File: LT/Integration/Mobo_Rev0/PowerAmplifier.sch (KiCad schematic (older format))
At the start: 12 parts, among them Q3 Q_NPN_BEC, Q4 Q_PNP_BEC, T1 TC2-1T+, T2 TC2-1T+

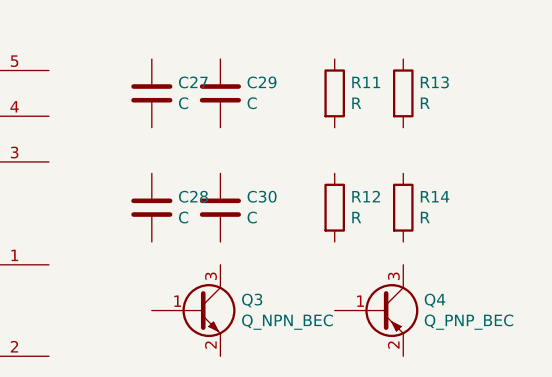
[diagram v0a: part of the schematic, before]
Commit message: I uploaded the schematics for the receiving stage into their respective hierarchial sheets and have begun the integration of the received stage
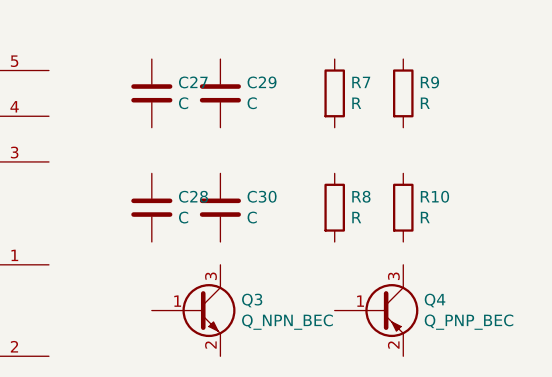
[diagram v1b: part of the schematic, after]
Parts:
- C27, C28, C29, C30: footprint Capacitor_SMD:C_0805_2012Metric -> (none)
- Q3, Q4: footprint Package_TO_SOT_SMD:SOT-23_Handsoldering -> (none)
- R10: renamed from R14; footprint Capacitor_SMD:C_0805_2012Metric -> (none)
- R7: renamed from R11; footprint Capacitor_SMD:C_0805_2012Metric -> (none)
- R8: renamed from R12; footprint Capacitor_SMD:C_0805_2012Metric -> (none)
- R9: renamed from R13; footprint Capacitor_SMD:C_0805_2012Metric -> (none)
- T1, T2: footprint Transformer_SMD:Transformer_MACOM_SM-22 -> (none)
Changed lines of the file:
@@
 F 0 "C27" H 4865 1446 50  0000 L CNN
 F 1 "C" H 4865 1355 50  0000 L CNN
-F 2 "Capacitor_SMD:C_0805_2012Metric" H 4788 1250 50  0001 C CNN
+F 2 "" H 4788 1250 50  0001 C CNN
 F 3 "~" H 4750 1400 50  0001 C CNN
 	1    4750 1400
@@
 F 0 "C29" H 5165 1446 50  0000 L CNN
 F 1 "C" H 5165 1355 50  0000 L CNN
-F 2 "Capacitor_SMD:C_0805_2012Metric" H 5088 1250 50  0001 C CNN
+F 2 "" H 5088 1250 50  0001 C CNN
 F 3 "~" H 5050 1400 50  0001 C CNN
 	1    5050 1400
@@
 F 0 "C28" H 4865 1946 50  0000 L CNN
 F 1 "C" H 4865 1855 50  0000 L CNN
-F 2 "Capacitor_SMD:C_0805_2012Metric" H 4788 1750 50  0001 C CNN
+F 2 "" H 4788 1750 50  0001 C CNN
 F 3 "~" H 4750 1900 50  0001 C CNN
 	1    4750 1900
@@
 F 0 "C30" H 5165 1946 50  0000 L CNN
 F 1 "C" H 5165 1855 50  0000 L CNN
-F 2 "Capacitor_SMD:C_0805_2012Metric" H 5088 1750 50  0001 C CNN
+F 2 "" H 5088 1750 50  0001 C CNN
 F 3 "~" H 5050 1900 50  0001 C CNN
 	1    5050 1900
@@
 $EndComp
 $Comp
-L Device:R R11
+L Device:R R7
 U 1 1 5E4C4AC0
 P 5550 1400
-F 0 "R11" H 5620 1446 50  0000 L CNN
+F 0 "R7" H 5620 1446 50  0000 L CNN
 F 1 "R" H 5620 1355 50  0000 L CNN
-F 2 "Capacitor_SMD:C_0805_2012Metric" V 5480 1400 50  0001 C CNN
+F 2 "" V 5480 1400 50  0001 C CNN
 F 3 "~" H 5550 1400 50  0001 C CNN
 	1    5550 1400
@@
 $EndComp
 $Comp
-L Device:R R13
+L Device:R R9
 U 1 1 5E4C4B1C
 P 5850 1400
-F 0 "R13" H 5920 1446 50  0000 L CNN
+F 0 "R9" H 5920 1446 50  0000 L CNN
 F 1 "R" H 5920 1355 50  0000 L CNN
-F 2 "Capacitor_SMD:C_0805_2012Metric" V 5780 1400 50  0001 C CNN
+F 2 "" V 5780 1400 50  0001 C CNN
 F 3 "~" H 5850 1400 50  0001 C CNN
 	1    5850 1400
@@
 $EndComp
 $Comp
-L Device:R R12
+L Device:R R8
 U 1 1 5E4C4B5D
 P 5550 1900
-F 0 "R12" H 5620 1946 50  0000 L CNN
+F 0 "R8" H 5620 1946 50  0000 L CNN
 F 1 "R" H 5620 1855 50  0000 L CNN
-F 2 "Capacitor_SMD:C_0805_2012Metric" V 5480 1900 50  0001 C CNN
+F 2 "" V 5480 1900 50  0001 C CNN
 F 3 "~" H 5550 1900 50  0001 C CNN
 	1    5550 1900
@@
 $EndComp
 $Comp
-L Device:R R14
+L Device:R R10
 U 1 1 5E4C4BA1
 P 5850 1900
-F 0 "R14" H 5920 1946 50  0000 L CNN
+F 0 "R10" H 5920 1946 50  0000 L CNN
 F 1 "R" H 5920 1855 50  0000 L CNN
-F 2 "Capacitor_SMD:C_0805_2012Metric" V 5780 1900 50  0001 C CNN
+F 2 "" V 5780 1900 50  0001 C CNN
 F 3 "~" H 5850 1900 50  0001 C CNN
 	1    5850 1900
@@
 F 0 "T1" H 3900 1878 50  0000 C CNN
 F 1 "TC2-1T+" H 3900 1787 50  0000 C CNN
-F 2 "Transformer_SMD:Transformer_MACOM_SM-22" H 3900 1500 50  0001 C CNN
+F 2 "" H 3900 1500 50  0001 C CNN
 F 3 "~" H 3900 1500 50  0001 C CNN
 	1    3900 1500
@@
 F 0 "T2" H 3900 2728 50  0000 C CNN
 F 1 "TC2-1T+" H 3900 2637 50  0000 C CNN
-F 2 "Transformer_SMD:Transformer_MACOM_SM-22" H 3900 2350 50  0001 C CNN
+F 2 "" H 3900 2350 50  0001 C CNN
 F 3 "~" H 3900 2350 50  0001 C CNN
 	1    3900 2350
@@
 F 0 "Q3" H 5141 2396 50  0000 L CNN
 F 1 "Q_NPN_BEC" H 5141 2305 50  0000 L CNN
-F 2 "Package_TO_SOT_SMD:SOT-23_Handsoldering" H 5150 2450 50  0001 C CNN
+F 2 "" H 5150 2450 50  0001 C CNN
 F 3 "~" H 4950 2350 50  0001 C CNN
 	1    4950 2350
@@
 F 0 "Q4" H 5940 2396 50  0000 L CNN
 F 1 "Q_PNP_BEC" H 5940 2305 50  0000 L CNN
-F 2 "Package_TO_SOT_SMD:SOT-23_Handsoldering" H 5950 2450 50  0001 C CNN
+F 2 "" H 5950 2450 50  0001 C CNN
 F 3 "~" H 5750 2350 50  0001 C CNN
 	1    5750 2350

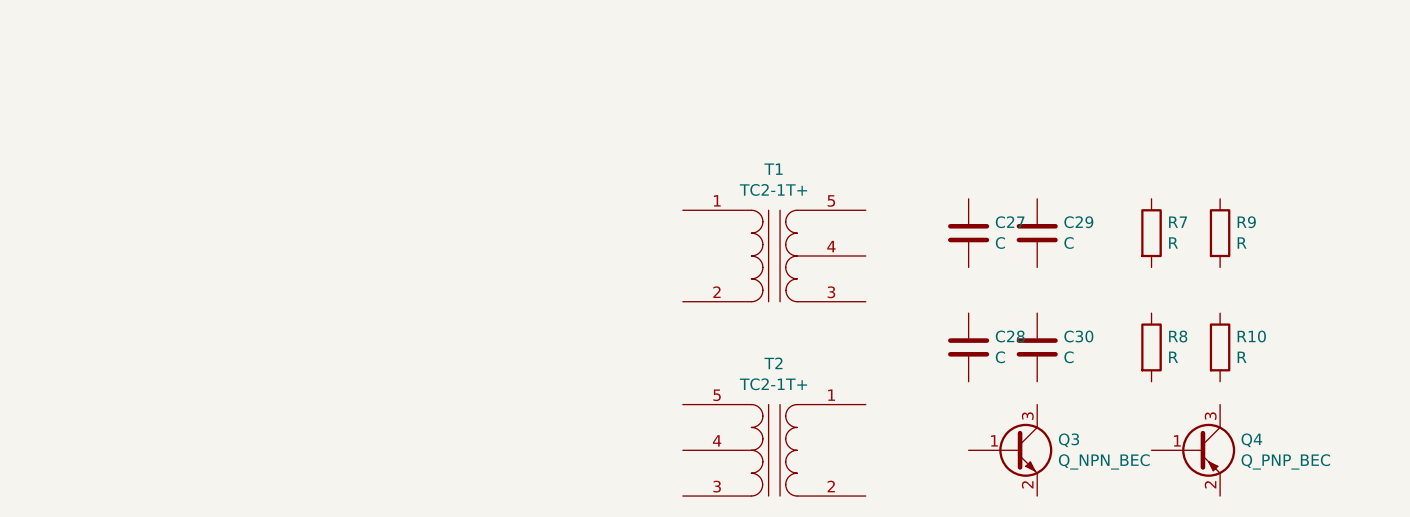
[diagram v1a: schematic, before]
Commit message: Uploaded Schematics to Integration of Phase 2
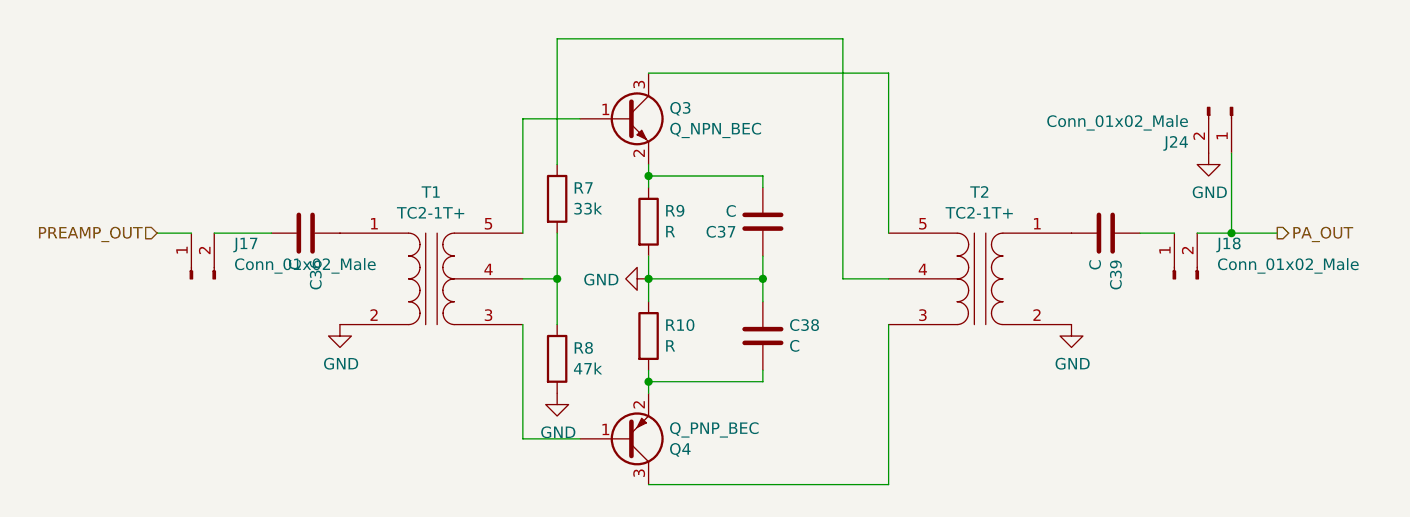
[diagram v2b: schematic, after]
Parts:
- added J17, J18: Conn_01x02_Male, Connector_PinHeader_2.54mm:PinHeader_1x02_P2.54mm_Vertical, symbol Connector:Conn_01x02_Male
- added J24: Conn_01x02_Male, Connector_Coaxial:SMA_Amphenol_132289_EdgeMount, symbol Connector:Conn_01x02_Male
- C36: renamed from C27; footprint (none) -> Capacitor_SMD:C_0805_2012Metric_Pad1.15x1.40mm_HandSolder
- C37: renamed from C28; footprint (none) -> Capacitor_SMD:C_0805_2012Metric_Pad1.15x1.40mm_HandSolder
- C38: renamed from C29; footprint (none) -> Capacitor_SMD:C_0805_2012Metric_Pad1.15x1.40mm_HandSolder
- C39: renamed from C30; footprint (none) -> Capacitor_SMD:C_0805_2012Metric_Pad1.15x1.40mm_HandSolder
- R7: value R -> 33k
- R8: value R -> 47k
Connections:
- net at C36.1: now also T1.1 (AA)
- net at C36.2: now also J17.2 (Pin_2)
- net GND: now reaches C38.1
- net GND: now also C37.1, R10.1, R8.2, R9.2, T1.2 (AB), T2.2 (AB), J24.2 (Pin_2)
- net at C38.2: now also Q4.2 (E), R10.2
- net at C37.2: now also Q3.2 (E), R9.1
- net at C39.1: now also J18.1 (Pin_1)
- net at C39.2: now also T2.1 (AA)
- net at R7.1: now also T2.4 (SC)
- net at R7.2: now also R8.1, T1.4 (SC)
- net at Q3.1 (B): now also T1.5 (SB)
- net at Q3.3 (C): now also T2.5 (SB)
- net at T1.3 (SA): now also Q4.1 (B)
- net at T2.3 (SA): now also Q4.3 (C)
- new net PA_OUT: J18.2 (Pin_2), J24.1 (Pin_1)
- new net PREAMP_OUT: J17.1 (Pin_1)
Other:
- moved on the sheet: C36, C37, C38, C39, Q3, Q4, R10, R7, R8, R9, T1, T2

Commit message: Finished PA PCB layout for transmitting stage. 3/4 blocks complete for integration
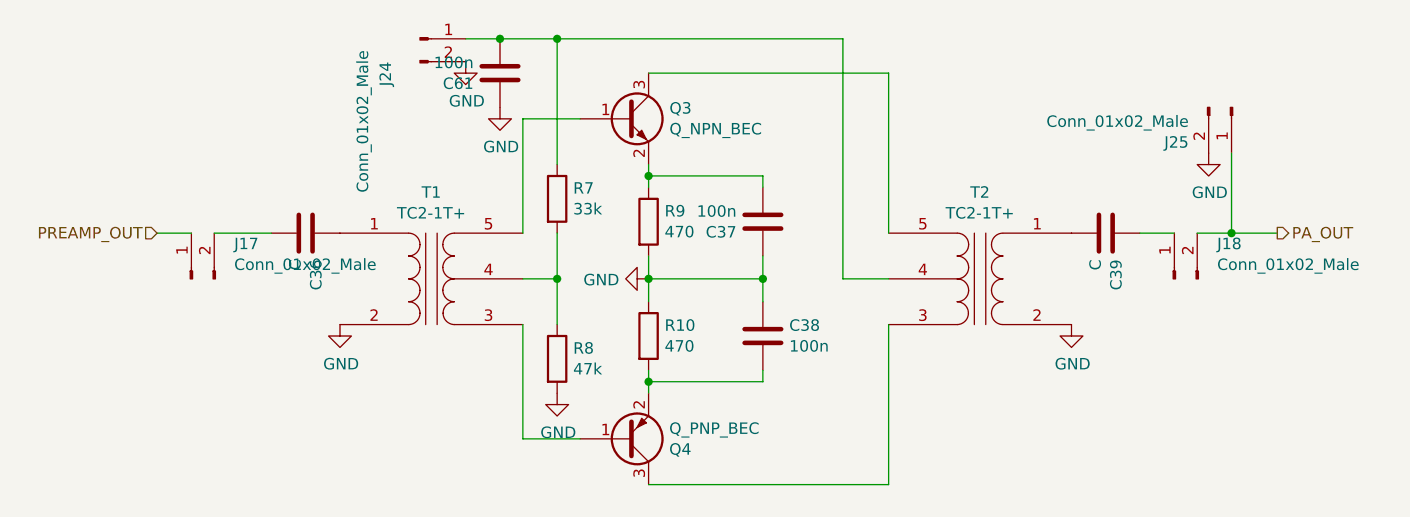
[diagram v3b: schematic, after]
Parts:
- added C61: 100n, Capacitor_SMD:C_0805_2012Metric_Pad1.15x1.40mm_HandSolder, symbol Device:C
- added J24: Conn_01x02_Male, Connector_PinHeader_2.54mm:PinHeader_1x02_P2.54mm_Vertical, symbol Connector:Conn_01x02_Male
- C37, C38: value C -> 100n
- R10, R9: value R -> 470
- renumbered J24 to J25
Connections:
- net GND: now also C61.1, J24.2 (Pin_2)
- net at R7.1, T2.4 (SC): now also C61.2, J24.1 (Pin_1)
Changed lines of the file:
@@
 P 3850 1850
 F 0 "C38" H 3965 1896 50  0000 L CNN
-F 1 "C" H 3965 1805 50  0000 L CNN
+F 1 "100n" H 3965 1805 50  0000 L CNN
 F 2 "Capacitor_SMD:C_0805_2012Metric_Pad1.15x1.40mm_HandSolder" H 3888 1700 50  0001 C CNN
 F 3 "~" H 3850 1850 50  0001 C CNN
@@
 P 3850 1350
 F 0 "C37" H 3965 1396 50  0000 L CNN
-F 1 "C" H 3965 1305 50  0000 L CNN
+F 1 "100n" H 3965 1305 50  0000 L CNN
 F 2 "Capacitor_SMD:C_0805_2012Metric_Pad1.15x1.40mm_HandSolder" H 3888 1200 50  0001 C CNN
 F 3 "~" H 3850 1350 50  0001 C CNN
@@
 P 3350 1350
 F 0 "R9" H 3420 1396 50  0000 L CNN
-F 1 "R" H 3420 1305 50  0000 L CNN
+F 1 "470" H 3420 1305 50  0000 L CNN
 F 2 "" V 3280 1350 50  0001 C CNN
 F 3 "~" H 3350 1350 50  0001 C CNN
@@
 P 3350 1850
 F 0 "R10" H 3420 1896 50  0000 L CNN
-F 1 "R" H 3420 1805 50  0000 L CNN
+F 1 "470" H 3420 1805 50  0000 L CNN
 F 2 "" V 3280 1850 50  0001 C CNN
 F 3 "~" H 3350 1850 50  0001 C CNN
@@
 	5500 1400 5650 1400
 $Comp
-L Connector:Conn_01x02_Male J24
+L Connector:Conn_01x02_Male J25
 U 1 1 5E9FE57C
 P 5900 850
-F 0 "J24" V 6053 663 50  0000 R CNN
+F 0 "J25" V 6053 663 50  0000 R CNN
 F 1 "Conn_01x02_Male" V 5962 663 50  0000 R CNN
 F 2 "Connector_Coaxial:SMA_Amphenol_132289_EdgeMount" H 5900 850 50  0001 C CNN
@@
 	1    0    0    -1
 $EndComp
+$Comp
+L Connector:Conn_01x02_Male J24
+U 1 1 5E9FB393
+P 2350 550
+F 0 "J24" V 2200 450 50  0000 R CNN
+F 1 "Conn_01x02_Male" V 2100 500 50  0000 R CNN
+F 2 "Connector_PinHeader_2.54mm:PinHeader_1x02_P2.54mm_Vertical" H 2350 550 50  0001 C CNN
+F 3 "~" H 2350 550 50  0001 C CNN
+	1    2350 550
+	1    0    0    -1
+$EndComp
+$Comp
+L Device:C C61
+U 1 1 5E9FC27C
+P 2700 700
+F 0 "C61" H 2815 746 50  0000 L CNN
+F 1 "100n" H 2815 655 50  0000 L CNN
+F 2 "Capacitor_SMD:C_0805_2012Metric_Pad1.15x1.40mm_HandSolder" H 2738 550 50  0001 C CNN
+F 3 "~" H 2700 700 50  0001 C CNN
+	1    2700 700
+	-1   0    0    1
+$EndComp
+Wire Wire Line
+	2550 550  2700 550
+Connection ~ 2950 550
+Connection ~ 2700 550
+Wire Wire Line
+	2700 550  2950 550
+$Comp
+L power:GND #PWR0121
+U 1 1 5E9FC7BC
+P 2700 850
+F 0 "#PWR0121" H 2700 600 50  0001 C CNN
+F 1 "GND" H 2705 677 50  0000 C CNN
+F 2 "" H 2700 850 50  0001 C CNN
+F 3 "" H 2700 850 50  0001 C CNN
+	1    2700 850
+	1    0    0    -1
+$EndComp
+$Comp
+L power:GND #PWR0122
+U 1 1 5E9FC7E9
+P 2550 650
+F 0 "#PWR0122" H 2550 400 50  0001 C CNN
+F 1 "GND" H 2555 477 50  0000 C CNN
+F 2 "" H 2550 650 50  0001 C CNN
+F 3 "" H 2550 650 50  0001 C CNN
+	1    2550 650
+	1    0    0    -1
+$EndComp
